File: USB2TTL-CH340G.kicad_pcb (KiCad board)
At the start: 2 copper layers, 18.4 x 30 mm, 21 parts, among them P1 PWR, P2 USB_OTG, P3 PWR_SEL, P4 CONN_01X06, U1 CH340G, X1 CRYSTAL_SMD

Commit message: 1.README中加入驱动链接及注意事项；2.更改R3电阻阻值为200欧姆；3.修改gitignore文件忽略bak文件。
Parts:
- R3: value 100 -> 200
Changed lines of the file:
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@@
       (effects (font (size 0.8 0.8) (thickness 0.15)))
     )
-    (fp_text value 100 (at 0.254 -1.397 90) (layer F.Fab)
+    (fp_text value 200 (at 0.254 -1.397 90) (layer F.Fab)
       (effects (font (size 0.8 0.8) (thickness 0.15)))
     )

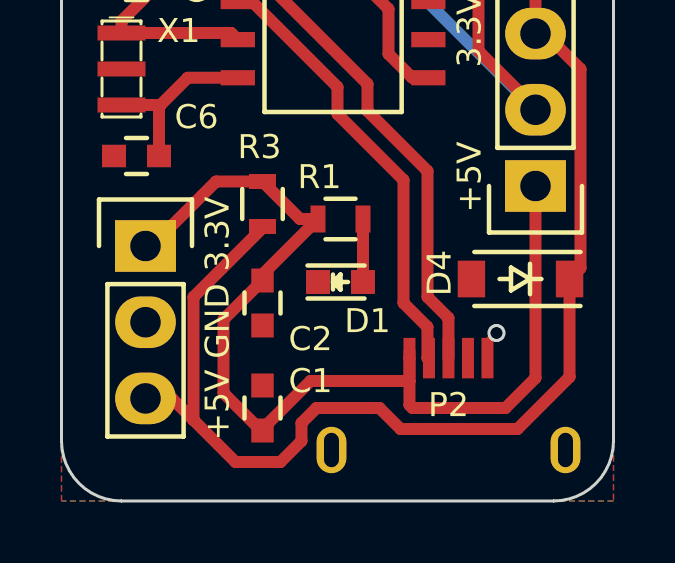
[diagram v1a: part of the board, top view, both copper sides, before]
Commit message: 修改micro usb封装，添加定位孔，更新pcb封装
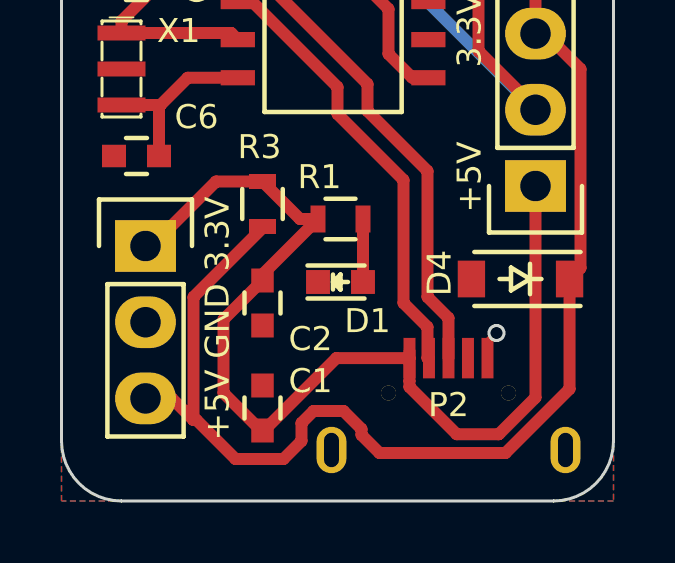
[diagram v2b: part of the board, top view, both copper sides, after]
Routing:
- net +5V: track 34.5 -> 35.6 mm
- net +3.3V: track 41.6 -> 42.4 mm
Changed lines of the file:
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@@
     (thickness 1.6)
     (drawings 23)
-    (tracks 128)
+    (tracks 132)
     (zones 0)
     (modules 21)
@@
     (mod_text_size 0.8 0.8)
     (mod_text_width 0.15)
-    (pad_size 1.35 0.4)
-    (pad_drill 0)
+    (pad_size 0.5 0.5)
+    (pad_drill 0.5)
     (pad_to_mask_clearance 0)
     (aux_axis_origin 135.6 102.6)
@@
     (add_net "Net-(U1-Pad15)")
     (add_net VCC)
-  )
-  (module myFootprints:USB_Micro-B-MK5 (layer F.Cu)
-    (at 148.5 129.4)
-    (descr "Micro USB Type B Receptacle")
-    (tags "USB USB_B USB_micro USB_OTG")
-    (attr smd)
-    (fp_text reference P2 (at 0 0) (layer F.SilkS)
-      (effects (font (size 0.8 0.8) (thickness 0.15)))
-    )
-    (fp_text value USB_OTG (at 0 1.778) (layer F.Fab)
-      (effects (font (size 0.8 0.8) (thickness 0.15)))
-    )
-    (fp_line (start -4.6 -2.8) (end 4.6 -2.8) (layer F.CrtYd) (width 0.05))
-    (fp_line (start 4.6 -2.8) (end 4.6 4.05) (layer F.CrtYd) (width 0.05))
-    (fp_line (start 4.6 4.05) (end -4.6 4.05) (layer F.CrtYd) (width 0.05))
-    (fp_line (start -4.6 4.05) (end -4.6 -2.8) (layer F.CrtYd) (width 0.05))
-    (pad 1 smd rect (at -1.3009 -1.56254 90) (size 1.35 0.4) (layers F.Cu F.Paste F.Mask)
-      (net 1 +5V))
-    (pad 2 smd rect (at -0.6509 -1.56254 90) (size 1.35 0.4) (layers F.Cu F.Paste F.Mask)
-      (net 19 "Net-(P2-Pad2)"))
-    (pad 3 smd rect (at -0.0009 -1.56254 90) (size 1.35 0.4) (layers F.Cu F.Paste F.Mask)
-      (net 20 "Net-(P2-Pad3)"))
-    (pad 4 smd rect (at 0.6491 -1.56254 90) (size 1.35 0.4) (layers F.Cu F.Paste F.Mask)
-      (net 21 "Net-(P2-Pad4)"))
-    (pad 5 smd rect (at 1.2991 -1.56254 90) (size 1.35 0.4) (layers F.Cu F.Paste F.Mask)
-      (net 2 GND))
-    (pad 6 thru_hole oval (at -3.9 1.5 90) (size 1.55 1) (drill oval 1.15 0.5) (layers *.Cu *.Mask F.SilkS)
-      (net 22 "Net-(P2-Pad6)"))
-    (pad 6 thru_hole oval (at 3.9 1.5 90) (size 1.55 1) (drill oval 1.15 0.5) (layers *.Cu *.Mask F.SilkS)
-      (net 22 "Net-(P2-Pad6)"))
   )
   (module Diodes_SMD:SOD-123 (layer F.Cu)
@@
     )
   )
+  (module myFootprints:USB_Micro-B-MK5 (layer F.Cu)
+    (at 148.5 129.4)
+    (descr "Micro USB Type B Receptacle")
+    (tags "USB USB_B USB_micro USB_OTG")
+    (attr smd)
+    (fp_text reference P2 (at 0 0) (layer F.SilkS)
+      (effects (font (size 0.8 0.8) (thickness 0.15)))
+    )
+    (fp_text value USB_OTG (at 0 1.778) (layer F.Fab)
+      (effects (font (size 0.8 0.8) (thickness 0.15)))
+    )
+    (fp_line (start -4.6 -2.8) (end 4.6 -2.8) (layer F.CrtYd) (width 0.05))
+    (fp_line (start 4.6 -2.8) (end 4.6 4.05) (layer F.CrtYd) (width 0.05))
+    (fp_line (start 4.6 4.05) (end -4.6 4.05) (layer F.CrtYd) (width 0.05))
+    (fp_line (start -4.6 4.05) (end -4.6 -2.8) (layer F.CrtYd) (width 0.05))
+    (pad 1 smd rect (at -1.3009 -1.56254 90) (size 1.35 0.4) (layers F.Cu F.Paste F.Mask)
+      (net 1 +5V))
+    (pad 2 smd rect (at -0.6509 -1.56254 90) (size 1.35 0.4) (layers F.Cu F.Paste F.Mask)
+      (net 19 "Net-(P2-Pad2)"))
+    (pad 3 smd rect (at -0.0009 -1.56254 90) (size 1.35 0.4) (layers F.Cu F.Paste F.Mask)
+      (net 20 "Net-(P2-Pad3)"))
+    (pad 4 smd rect (at 0.6491 -1.56254 90) (size 1.35 0.4) (layers F.Cu F.Paste F.Mask)
+      (net 21 "Net-(P2-Pad4)"))
+    (pad 5 smd rect (at 1.2991 -1.56254 90) (size 1.35 0.4) (layers F.Cu F.Paste F.Mask)
+      (net 2 GND))
+    (pad 6 thru_hole oval (at -3.9 1.5 90) (size 1.55 1) (drill oval 1.15 0.5) (layers *.Cu *.Mask F.SilkS)
+      (net 22 "Net-(P2-Pad6)"))
+    (pad 6 thru_hole oval (at 3.9 1.5 90) (size 1.55 1) (drill oval 1.15 0.5) (layers *.Cu *.Mask F.SilkS)
+      (net 22 "Net-(P2-Pad6)"))
+    (pad "" thru_hole circle (at 2 -0.4) (size 0.5 0.5) (drill 0.5) (layers *.Cu *.Mask F.SilkS)
+      (zone_connect 0))
+    (pad "" thru_hole circle (at -2 -0.4) (size 0.5 0.5) (drill 0.5) (layers *.Cu *.Mask F.SilkS)
+      (zone_connect 0))
+  )
   (gr_text SMSLIT (at 144.5 117.2 180) (layer B.SilkS)
     (effects (font (size 2 2) (thickness 0.3)) (justify mirror))
@@
     (effects (font (size 0.8 0.8) (thickness 0.15)))
   )
+  (segment (start 144.76254 127.83746) (end 147.1991 127.83746) (width 0.4) (layer F.Cu) (net 1))
+  (segment (start 142.35 130.25) (end 144.76254 127.83746) (width 0.4) (layer F.Cu) (net 1))
+  (segment (start 142.3 130.25) (end 142.35 130.25) (width 0.4) (layer F.Cu) (net 1))
+  (segment (start 147.1991 128.6) (end 147.1991 128.7991) (width 0.4) (layer F.Cu) (net 1))
+  (segment (start 151.4 129.15147) (end 151.4 122.1) (width 0.4) (layer F.Cu) (net 1))
+  (segment (start 150.175735 130.375735) (end 151.4 129.15147) (width 0.4) (layer F.Cu) (net 1))
+  (segment (start 148.775735 130.375735) (end 150.175735 130.375735) (width 0.4) (layer F.Cu) (net 1))
+  (segment (start 147.1991 128.7991) (end 148.775735 130.375735) (width 0.4) (layer F.Cu) (net 1))
   (segment (start 142.3 125.25) (end 142.3 125.05) (width 0.4) (layer F.Cu) (net 1))
   (segment (start 142.3 125.05) (end 144.15 123.2) (width 0.4) (layer F.Cu) (net 1))
@@
   (segment (start 140.75 121.95) (end 142.3 121.95) (width 0.4) (layer F.Cu) (net 1))
   (segment (start 142.3 130.25) (end 142.3 130.2) (width 0.4) (layer F.Cu) (net 1))
-  (segment (start 142.3 130.2) (end 143.9 128.6) (width 0.4) (layer F.Cu) (net 1))
-  (segment (start 143.9 128.6) (end 147.1991 128.6) (width 0.4) (layer F.Cu) (net 1))
   (segment (start 142.3 130.25) (end 142.25 130.25) (width 0.4) (layer F.Cu) (net 1))
   (segment (start 142.25 130.25) (end 141 129) (width 0.4) (layer F.Cu) (net 1))
   (segment (start 141 126.55) (end 142.3 125.25) (width 0.4) (layer F.Cu) (net 1))
   (segment (start 141 129) (end 141 126.55) (width 0.4) (layer F.Cu) (net 1))
-  (segment (start 151.4 122.1) (end 151.4 128.5) (width 0.4) (layer F.Cu) (net 1))
-  (segment (start 147.1991 129.3991) (end 147.1991 128.6) (width 0.4) (layer F.Cu) (net 1))
   (segment (start 147.1991 128.6) (end 147.1991 127.83746) (width 0.4) (layer F.Cu) (net 1))
-  (segment (start 147.3 129.5) (end 147.1991 129.3991) (width 0.4) (layer F.Cu) (net 1))
-  (segment (start 150.4 129.5) (end 147.3 129.5) (width 0.4) (layer F.Cu) (net 1))
-  (segment (start 151.4 128.5) (end 150.4 129.5) (width 0.4) (layer F.Cu) (net 1))
   (segment (start 147.1991 127.83746) (end 147.1991 127.5991) (width 0.4) (layer F.Cu) (net 1))
   (segment (start 149.7991 127.83746) (end 149.7991 127.3009) (width 0.25) (layer F.Cu) (net 2))
@@
   (segment (start 147.291 118.491) (end 146.5 117.7) (width 0.4) (layer F.Cu) (net 12))
   (segment (start 147.828 118.491) (end 147.291 118.491) (width 0.4) (layer F.Cu) (net 12))
+  (segment (start 140 129.9) (end 140.1 129.9) (width 0.4) (layer F.Cu) (net 18))
+  (segment (start 152.535 128.865) (end 152.535 125.2) (width 0.4) (layer F.Cu) (net 18))
+  (segment (start 150.4 131) (end 152.535 128.865) (width 0.4) (layer F.Cu) (net 18))
+  (segment (start 146.2 131) (end 150.4 131) (width 0.4) (layer F.Cu) (net 18))
+  (segment (start 145.6 130.4) (end 146.2 131) (width 0.4) (layer F.Cu) (net 18))
+  (segment (start 145.6 130.2) (end 145.6 130.4) (width 0.4) (layer F.Cu) (net 18))
+  (segment (start 145 129.6) (end 145.6 130.2) (width 0.4) (layer F.Cu) (net 18))
+  (segment (start 144 129.6) (end 145 129.6) (width 0.4) (layer F.Cu) (net 18))
+  (segment (start 143.6 130) (end 144 129.6) (width 0.4) (layer F.Cu) (net 18))
+  (segment (start 143.6 130.6) (end 143.6 130) (width 0.4) (layer F.Cu) (net 18))
+  (segment (start 143 131.2) (end 143.6 130.6) (width 0.4) (layer F.Cu) (net 18))
+  (segment (start 141.4 131.2) (end 143 131.2) (width 0.4) (layer F.Cu) (net 18))
+  (segment (start 140.1 129.9) (end 141.4 131.2) (width 0.4) (layer F.Cu) (net 18))
   (segment (start 142.3 123.45) (end 142.3 123.5) (width 0.4) (layer F.Cu) (net 18))
   (segment (start 142.3 123.5) (end 140 125.8) (width 0.4) (layer F.Cu) (net 18))
@@
   (segment (start 138.4 129.18) (end 139.28 129.18) (width 0.4) (layer F.Cu) (net 18))
   (segment (start 139.28 129.18) (end 140 129.9) (width 0.4) (layer F.Cu) (net 18))
-  (segment (start 140 129.9) (end 141.4 131.3) (width 0.4) (layer F.Cu) (net 18))
-  (segment (start 152.535 128.465) (end 152.535 125.2) (width 0.4) (layer F.Cu) (net 18))
-  (segment (start 150.8 130.2) (end 152.535 128.465) (width 0.4) (layer F.Cu) (net 18))
-  (segment (start 146.9 130.2) (end 150.8 130.2) (width 0.4) (layer F.Cu) (net 18))
-  (segment (start 146.2 129.5) (end 146.9 130.2) (width 0.4) (layer F.Cu) (net 18))
-  (segment (start 144.1 129.5) (end 146.2 129.5) (width 0.4) (layer F.Cu) (net 18))
-  (segment (start 143.6 130) (end 144.1 129.5) (width 0.4) (layer F.Cu) (net 18))
-  (segment (start 143.6 130.6) (end 143.6 130) (width 0.4) (layer F.Cu) (net 18))
-  (segment (start 142.9 131.3) (end 143.6 130.6) (width 0.4) (layer F.Cu) (net 18))
-  (segment (start 141.4 131.3) (end 142.9 131.3) (width 0.4) (layer F.Cu) (net 18))
   (segment (start 150.95 112.8) (end 150.85 112.7) (width 0.4) (layer F.Cu) (net 18))
   (segment (start 141.478 115.951) (end 141.951 115.951) (width 0.4) (layer F.Cu) (net 19))

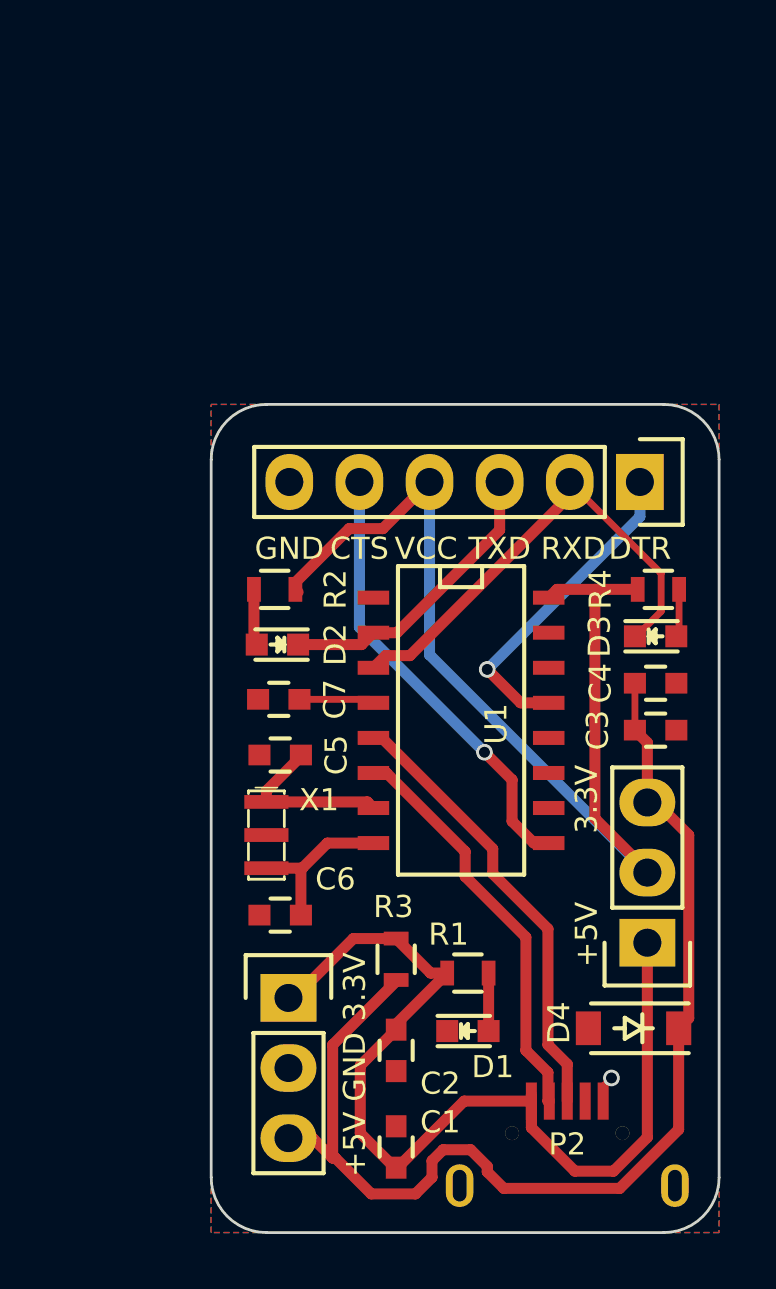
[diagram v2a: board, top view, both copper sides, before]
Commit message: 删掉对外供电的插针，重新布局设计PCB，大小为25mmX18mm，并导出单板的gerber文件和钻孔文件
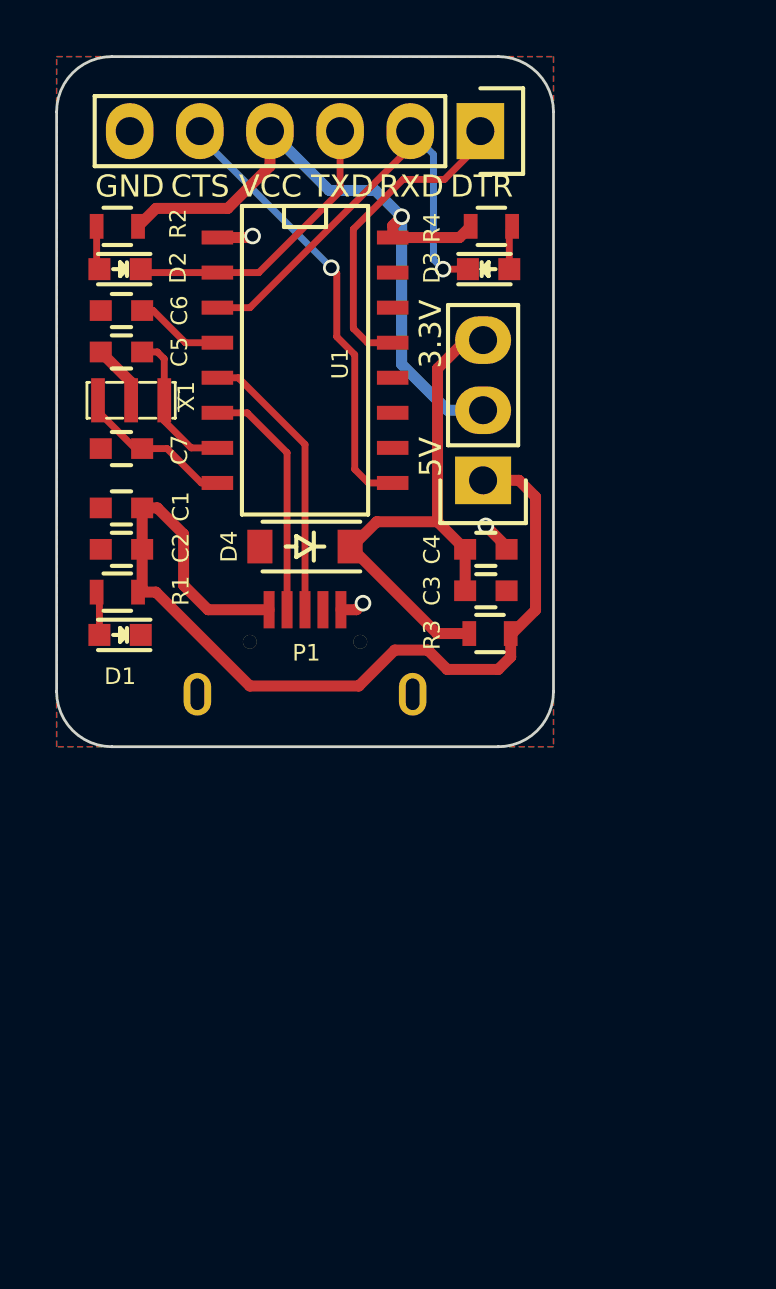
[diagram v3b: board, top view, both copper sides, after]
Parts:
- removed P4: CONN_01X06, Pin_Headers:Pin_Header_Straight_1x06
- C6: value 22pF -> 0.01uF
- C7: value 0.01uF -> 22pF
- P1: value PWR -> USB_OTG; footprint Pin_Headers:Pin_Header_Straight_1x03 -> myFootprints:USB_Micro-B-MK5
- P2: value USB_OTG -> PWR_SEL; footprint myFootprints:USB_Micro-B-MK5 -> Pin_Headers:Pin_Header_Straight_1x03
- P3: value PWR_SEL -> CONN_01X06; footprint Pin_Headers:Pin_Header_Straight_1x03 -> Pin_Headers:Pin_Header_Straight_1x06
- X1: footprint Crystals:Resonator_3.2x1.5mm -> myFootprints:Resonator_3.2x1.5mm
- moved P3 30.0 mm to (145.3, 92.7), turned to 270 degrees
- moved C1 25.2 mm to (132.3, 106.3), turned to 180 degrees
- moved P2 24.2 mm to (145.4, 105.3), turned to 180 degrees
- moved C6 22.6 mm to (132.3, 99.2)
- moved D4 21.1 mm to (139.0, 107.8)
- moved C2 20.7 mm to (132.3, 107.8), turned to 180 degrees
- moved D1 19.1 mm to (132.3, 111.0), turned to 180 degrees
- moved R1 18.8 mm to (132.2, 109.4), turned to 0 degrees
- moved X1 16.5 mm to (132.7, 102.5), turned to 180 degrees
- moved C5 15.7 mm to (132.3, 100.7)
- moved D2 14.7 mm to (132.3, 97.7)
- moved D3 14.6 mm to (145.7, 97.7)
- moved R4 14.5 mm to (145.8, 96.2)
- moved R2 14.3 mm to (132.2, 96.2)
- moved U1 14.2 mm to (139.0, 101.0)
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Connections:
- P1 pad 2: GND -> Net-(P1-Pad2)
- P1 pad 3: +3.3V -> Net-(P1-Pad3)
- P2 pad 2: Net-(P2-Pad2) -> VCC
- P2 pad 3: Net-(P2-Pad3) -> +3.3V
- P3 pad 1: +5V -> /DTR
- P3 pad 2: VCC -> /RXD
- P3 pad 3: +3.3V -> /TXD
- U1 pad 4: Net-(C7-Pad1) -> Net-(C6-Pad1)
- U1 pad 5: Net-(P2-Pad3) -> Net-(P1-Pad3)
- U1 pad 6: Net-(P2-Pad2) -> Net-(P1-Pad2)
- U1 pad 8: Net-(C6-Pad1) -> Net-(C7-Pad1)
- X1 pad 2: Net-(C6-Pad1) -> Net-(C7-Pad1)
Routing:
- net +3.3V: track 42.4 -> 19.7 mm
- net Net-(P2-Pad3): track 16.2 -> 0.00 mm
- net Net-(P2-Pad2): track 14.8 -> 0.00 mm
- net VCC: track 39.1 -> 25.9 mm, vias 0 -> 1
- net Net-(P1-Pad3): track 0.00 -> 10.2 mm
- net Net-(P1-Pad2): track 0.00 -> 8.81 mm
- net GND: track 1.18 -> 5.56 mm, vias 1 -> 3
- net Net-(C7-Pad1): track 2.73 -> 5.80 mm
- net Net-(C6-Pad1): track 6.00 -> 3.21 mm
- net /RXD: track 18.2 -> 16.4 mm, vias 0 -> 1
- net /DTR: track 13.0 -> 11.6 mm, vias 1 -> 0
- net +5V: track 35.6 -> 34.6 mm
- net Net-(D2-Pad2): track 2.38 -> 1.59 mm
- net Net-(C5-Pad1): track 6.19 -> 5.48 mm
- net Net-(D1-Pad2): track 2.24 -> 1.59 mm
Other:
- board size 18.4 x 30 mm -> 18 x 25 mm
- board text added: "5V"
- board text removed: "+5V"
- board text removed: "SMSLIT"
- board text removed: "by 5km"

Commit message: 1.新建myRegul库并添加元件LDO芯片XP6206；2.用最大可提供500mA电流的XP6206替换掉原来的二极管稳压电路，提高稳定性；3.调整PCB元件布局。
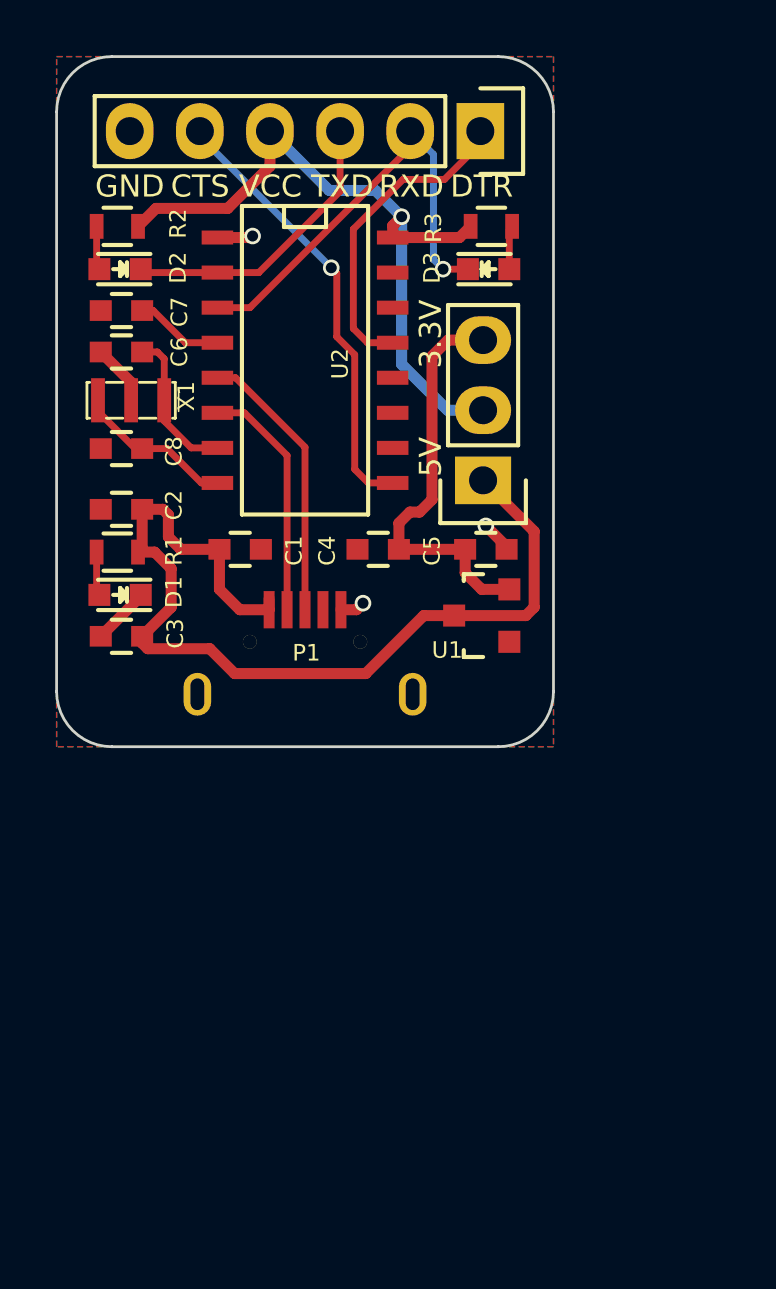
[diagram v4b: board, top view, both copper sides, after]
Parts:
- removed D4: 3V3, Diodes_SMD:SOD-123
- removed R4: 4.7K, Resistors_SMD:R_0603
- added C8: 22pF, Capacitors_SMD:C_0603, F.Cu at (132.3, 104.2)
- added U2: CH340G, SMD_Packages:SO-16-N, F.Cu at (139.0, 101.0)
- C3: value 0.1uF -> 1uF
- C4: value 10uF -> 0.1uF
- C5: value 22pF -> 1uF
- C6: value 0.01uF -> 22pF
- C7: value 22pF -> 0.01uF
- R3: value 200 -> 4.7K
- U1: value CH340G -> XC6206P332MR; footprint SMD_Packages:SO-16-N -> TO_SOT_Packages_SMD:SOT-23
- moved C5 15.0 mm to (145.6, 107.8), turned to 0 degrees
- moved R3 14.8 mm to (145.8, 96.2)
- moved C3 13.3 mm to (132.3, 111.0), turned to 180 degrees
- moved U1 11.2 mm to (145.4, 110.2), turned to 90 degrees
- moved C7 5.00 mm to (132.3, 99.2)
- moved C1 4.55 mm to (136.7, 107.8), turned to 0 degrees
- moved C4 3.90 mm to (141.7, 107.8), turned to 180 degrees
- moved C6 1.50 mm to (132.3, 100.7)
- moved D1 1.45 mm to (132.3, 109.5)
- moved R1 1.45 mm to (132.2, 108.0)
- moved C2 1.45 mm to (132.3, 106.4)
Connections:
- C3 pad 1: +3.3V -> +5V
- C5 pad 1: Net-(C5-Pad1) -> +3.3V
- P1 pad 4: Net-(P1-Pad4) -> (no net)
- R3 pad 1: +3.3V -> VCC
- R3 pad 2: +5V -> Net-(D3-Pad2)
- U1 pad 2: /TXD -> +3.3V
- U1 pad 3: /RXD -> +5V
- X1 pad 1: Net-(C5-Pad1) -> Net-(C6-Pad1)
- X1 pad 2: Net-(C7-Pad1) -> Net-(C8-Pad1)
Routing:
- net Net-(C8-Pad1): track 0.00 -> 5.80 mm
- net Net-(C5-Pad1): track 5.48 -> 0.00 mm
- net +3.3V: track 19.7 -> 15.5 mm
- net Net-(C7-Pad1): track 5.80 -> 3.21 mm
- net Net-(C6-Pad1): track 3.21 -> 5.48 mm
- net GND: track 5.56 -> 7.66 mm
